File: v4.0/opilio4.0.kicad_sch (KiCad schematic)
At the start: 81 parts, among them J1 Screw_Terminal_01x02, J2 Conn_01x02_Male, J3 USB_B_Micro, J5 Conn_01x02_Male, Q1 PMV25ENEAR, Q2 PMV25ENEAR, U1 AMS1117-3.3, U5 STM32F103C8T6, Y1 YSX531SL 8MHz, Y2 YST310S 32.768KHz

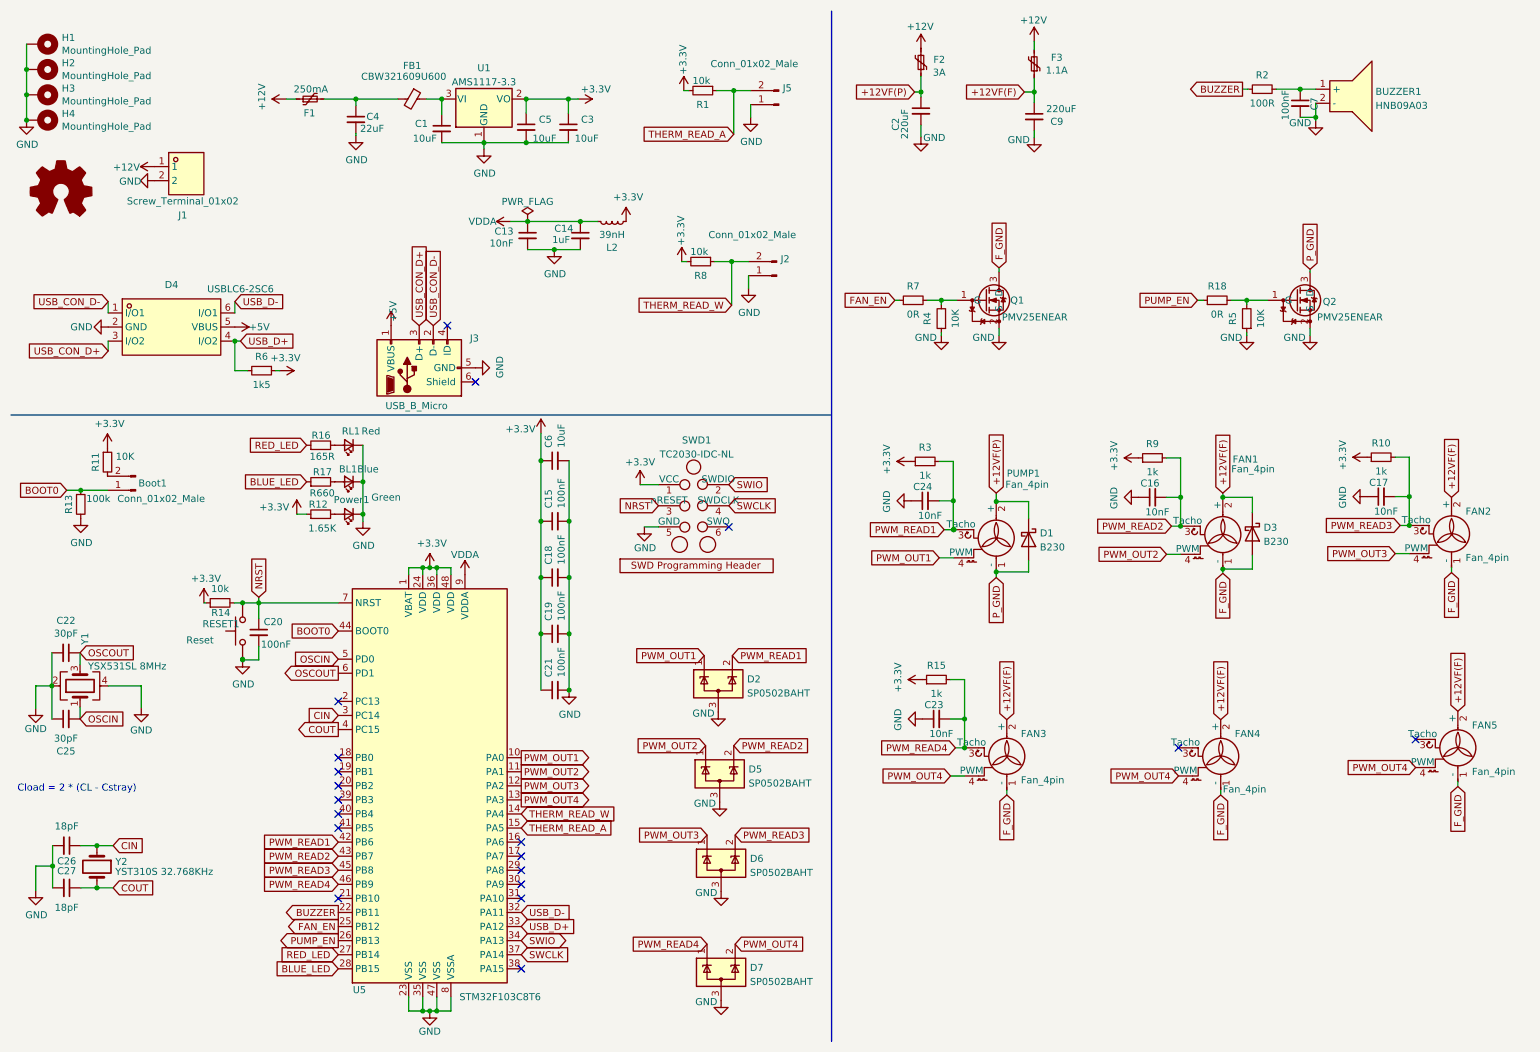
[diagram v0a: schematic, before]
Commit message: initial board without mosfets
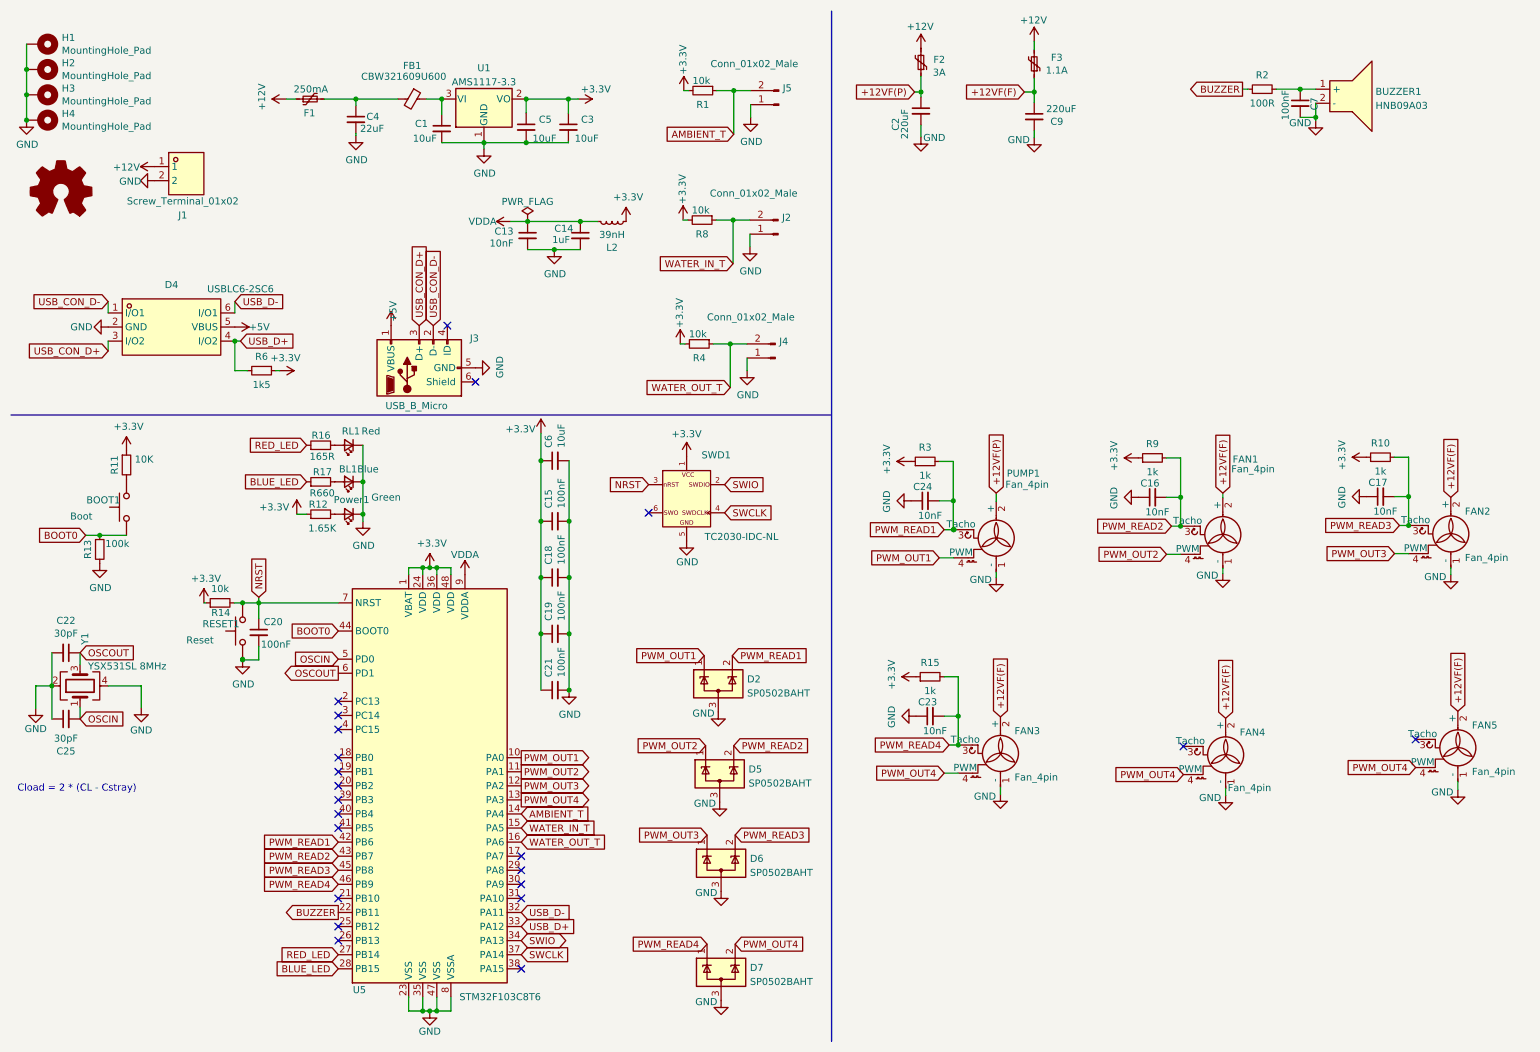
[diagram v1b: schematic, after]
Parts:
- removed Boot1: Conn_01x02_Male, Connector_PinHeader_2.54mm:PinHeader_1x02_P2.54mm_Vertical, symbol Connector:Conn_01x02_Male
- removed C26, C27: 18pF, Capacitor_SMD:C_0603_1608Metric_Pad1.08x0.95mm_HandSolder, symbol Device:C_Small
- removed D1, D3: B230, Diode_SMD:D_SMB, symbol Diode:B230
- removed Q1, Q2: PMV25ENEAR, easyeda2kicad:SOT-23_L2.9-W1.3-P1.90-LS2.4-BR, symbol easyeda:PMV25ENEAR
- removed R18, R7: 0R, Resistor_SMD:R_0603_1608Metric_Pad0.98x0.95mm_HandSolder, symbol Device:R_Small
- removed R5: 10K, Resistor_SMD:R_0603_1608Metric_Pad0.98x0.95mm_HandSolder, symbol Device:R_Small
- removed Y2: YST310S 32.768KHz, Crystal:Crystal_SMD_3215-2Pin_3.2x1.5mm, symbol Device:Crystal
- added BOOT1: Boot, easyeda2kicad:SW-SMD_L6.0-W3.3-LS8.0, symbol Switch:SW_Push
- added J4: Conn_01x02_Male, Connector_PinHeader_2.54mm:PinHeader_1x02_P2.54mm_Vertical, symbol Connector:Conn_01x02_Male
- R4: value 10K -> 10k
- RESET1: footprint easyedakicad:SW-SMD_L6.0-W3.3-LS8.0 -> easyeda2kicad:SW-SMD_L6.0-W3.3-LS8.0
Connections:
- net F_GND is gone; now on net GND: FAN1.1 (-), FAN2.1 (-), FAN3.1 (-), FAN4.1 (-), FAN5.1 (-)
- net P_GND is gone; now on net GND: PUMP1.1 (-)
- net +3.3V: now also R4.2
- net BOOT0: now also BOOT1.1
- net GND: now also J4.1 (Pin_1); no longer R4.1
- net WATER_OUT_T: now reaches U5.16 (PA6)
- net WATER_OUT_T: now also R4.1, J4.2 (Pin_2)
- net at R11.2: now also BOOT1.2
- net CIN: no longer names the net of U5.3 (PC14)
- net COUT: no longer names the net of U5.4 (PC15)
- net FAN_EN: no longer names the net of U5.25 (PB12)
- net PUMP_EN: no longer names the net of U5.26 (PB13)
- net THERM_READ_A renamed AMBIENT_T
- net AMBIENT_T: now also U5.14 (PA4); no longer U5.15 (PA5)
- net THERM_READ_W renamed WATER_IN_T
- net WATER_IN_T: now also U5.15 (PA5); no longer U5.14 (PA4)
- no-connect marks 19 -> 22
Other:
- moved on the sheet: C23, FAN3, FAN4, J2, R11, R13, R15, R8

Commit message: cleanup and reroute
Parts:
- removed C1, C3: 10uF, Capacitor_SMD:C_0603_1608Metric_Pad1.08x0.95mm_HandSolder, symbol Device:C_Small
- removed U1: AMS1117-3.3, Package_TO_SOT_SMD:SOT-223-3_TabPin2, symbol Regulator_Linear:AMS1117-3.3
- added C13, C14: 10uF, Capacitor_SMD:C_0603_1608Metric_Pad1.08x0.95mm_HandSolder, symbol Device:C_Small
- added C22, C23: 18pF, Capacitor_SMD:C_0603_1608Metric_Pad1.08x0.95mm_HandSolder, symbol Device:C_Small
- added D2, D7: B230A, Diode_SMD:D_SMA, symbol Device:D_Schottky_Small
- added L1: 4.7uH, Inductor_SMD:L_Bourns-SRN4018, symbol Device:L_Small
- added R10: 24k, Resistor_SMD:R_0603_1608Metric_Pad0.98x0.95mm_HandSolder, symbol Device:R_Small
- added R8: 22R, Resistor_SMD:R_0603_1608Metric_Pad0.98x0.95mm_HandSolder, symbol Device:R_Small
- added R9: 75k, Resistor_SMD:R_0603_1608Metric_Pad0.98x0.95mm_HandSolder, symbol Device:R_Small
- added TP1: 3v3, TestPoint:TestPoint_Pad_D1.0mm, symbol Connector:TestPoint
- added U1: EUP3458, Package_TO_SOT_SMD:SOT-23-6_Handsoldering, symbol Custom:EUP3458
- added Y2: YST310S 32.768KHz, Crystal:Crystal_SMD_3215-2Pin_3.2x1.5mm, symbol Device:Crystal
- C4: value 22uF -> 10uF; footprint Capacitor_SMD:C_1206_3216Metric_Pad1.33x1.80mm_HandSolder -> Capacitor_SMD:C_0603_1608Metric_Pad1.08x0.95mm_HandSolder
- C5: value 10uF -> 10nF
- renumbered C22 to C1, C19 to C10, C21 to C11, C14 to C12, C2 to C15, C24 to C16, C23 to C17, C9 to C18, C16 to C19, C25 to C2, C7 to C20, C17 to C21, C20 to C3, C13 to C6, C6 to C7, C15 to C8, C18 to C9, D4 to D1, D2 to D3, D5 to D4, D6 to D5, D7 to D6, FAN1 to FAN2, FAN2 to FAN3, FAN3 to FAN4, FAN4 to FAN5, FAN5 to FAN6, J3 to J2, J5 to J3, J2 to J4, J4 to J5, R13 to R1, R1 to R11, R3 to R12, R15 to R13, R8 to R14, R9 to R15, R2 to R16, R4 to R17, R10 to R18, R11 to R2, R14 to R3, R6 to R4, R16 to R5, R17 to R6, R12 to R7, U5 to U2
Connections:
- net +12V: now also D7.1 (K)
- net +3.3V: now also C13.1, C14.1, L1.2, R9.1, TP1.1; no longer C5.1
- net GND: now also C13.2, C14.2, C22.2, C23.2, D2.2 (A), D7.2 (A), R10.2, U1.2 (GND); no longer C5.2
- net at FB1.1: now also C4.1, R8.1, U1.5 (IN)
- net CIN: now reaches U2.3 (PC14)
- net CIN: now also C22.1, Y2.1
- net COUT: now reaches U2.4 (PC15)
- net COUT: now also C23.1, Y2.2
- net at F1.2, FB1.2: no longer C4.1
- new net: C5.1, D2.1 (K), L1.1, U1.6 (SW)
- new net: C5.2, U1.1 (BST)
- new net: R8.2, U1.4 (EN)
- new net BUCK_FB: R10.1, R9.2, U1.3 (FB)
- no-connect marks 22 -> 20
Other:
- moved on the sheet: J3, J4, J5, R11, R14, R17
